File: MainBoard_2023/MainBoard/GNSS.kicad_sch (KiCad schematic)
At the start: 16 parts

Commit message: 裏面にSDスロットを配置、GPS配置
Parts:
- removed JP4: SolderJumper, Jumper:SolderJumper-3_P2.0mm_Open_TrianglePad1.0x1.5mm_NumberLabels, symbol Jumper:SolderJumper_3_Bridged123
- removed R46, R47: 470, Resistor_SMD:R_0603_1608Metric_Pad0.98x0.95mm_HandSolder, symbol Device:R_Small
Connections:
- net +3.3V: now also R48.2, R49.2
- net RX: now also ANT1.14 (RXD)
- net TX: now also ANT1.13 (TXD)
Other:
- note removed: "Cut Jumper to remove I2C pullups from bus"
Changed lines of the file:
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@@
   (junction (at 146.05 78.74) (diameter 0) (color 0 0 0 0)
   )
+  (junction (at 195.58 73.66) (diameter 0) (color 0 0 0 0)
+  )
   (junction (at 190.5 88.9) (diameter 0) (color 0 0 0 0)
   )
@@
     (stroke (width 0) (type default) (color 0 0 0 0))
   )
-  (wire (pts (xy 195.58 67.31) (xy 195.58 69.85))
+  (wire (pts (xy 195.58 72.39) (xy 195.58 73.66))
     (stroke (width 0) (type default) (color 0 0 0 0))
   )
@@
     (stroke (width 0) (type default) (color 0 0 0 0))
   )
-  (wire (pts (xy 172.72 96.52) (xy 177.8 96.52))
+  (wire (pts (xy 172.72 96.52) (xy 180.34 96.52))
+    (stroke (width 0) (type default) (color 0 0 0 0))
+  )
+  (wire (pts (xy 190.5 73.66) (xy 195.58 73.66))
     (stroke (width 0) (type default) (color 0 0 0 0))
   )
@@
     (stroke (width 0) (type default) (color 0 0 0 0))
   )
-  (wire (pts (xy 182.88 93.98) (xy 185.42 93.98))
-    (stroke (width 0) (type default) (color 0 0 0 0))
-  )
-  (wire (pts (xy 182.88 96.52) (xy 185.42 96.52))
+  (wire (pts (xy 195.58 73.66) (xy 200.66 73.66))
     (stroke (width 0) (type default) (color 0 0 0 0))
   )
@@
     (stroke (width 0) (type default) (color 0 0 0 0))
   )
-  (wire (pts (xy 172.72 93.98) (xy 177.8 93.98))
+  (wire (pts (xy 172.72 93.98) (xy 180.34 93.98))
     (stroke (width 0) (type default) (color 0 0 0 0))
   )
@@
     (effects (font (size 1 1)) (justify left bottom))
   )
-  (text "Cut Jumper to remove\nI2C pullups from bus" (at 176.53 71.12 180)
-    (effects (font (size 1 1)) (justify left bottom))
-  )
   (text "RTC Backup" (at 115.57 62.23 180)
     (effects (font (size 2.54 2.54)) (justify right bottom))
@@
     (effects (font (size 1.27 1.27)) (justify right bottom))
   )
-  (hierarchical_label "TX" (shape passive) (at 185.42 93.98 0)
+  (hierarchical_label "TX" (shape passive) (at 180.34 93.98 0)
     (effects (font (size 1.27 1.27)) (justify left))
   )
@@
     (effects (font (size 1.27 1.27)) (justify left))
   )
-  (hierarchical_label "RX" (shape passive) (at 185.42 96.52 0)
-    (effects (font (size 1.27 1.27)) (justify left))
-  )
-  (symbol (lib_id "Device:R_Small") (at 180.34 96.52 90) (unit 1)
-    (in_bom yes) (on_board yes)
-    (property "Reference" "R47" (id 0) (at 176.53 97.79 90))
-    (property "Value" "470" (id 1) (at 180.34 96.52 90))
-    (property "Footprint" "Resistor_SMD:R_0603_1608Metric_Pad0.98x0.95mm_HandSolder" (id 2) (at 180.34 96.52 0)
-      (effects (font (size 1.27 1.27)) hide)
-    )
-    (property "Datasheet" "~" (id 3) (at 180.34 96.52 0)
-      (effects (font (size 1.27 1.27)) hide)
-    )
-    (pin "1")
-    (pin "2")
-  )
-  (symbol (lib_id "power:+3.3V") (at 195.58 67.31 0) (unit 1)
-    (in_bom yes) (on_board yes)
-    (property "Reference" "#PWR0110" (id 0) (at 195.58 71.12 0)
-      (effects (font (size 1.27 1.27)) hide)
-    )
-    (property "Value" "+3.3V" (id 1) (at 195.58 63.5 0))
-    (property "Footprint" "" (id 2) (at 195.58 67.31 0)
-      (effects (font (size 1.27 1.27)) hide)
-    )
-    (property "Datasheet" "" (id 3) (at 195.58 67.31 0)
+  (hierarchical_label "RX" (shape passive) (at 180.34 96.52 0)
+    (effects (font (size 1.27 1.27)) (justify left))
+  )
+  (symbol (lib_id "power:+3.3V") (at 195.58 72.39 0) (unit 1)
+    (in_bom yes) (on_board yes)
+    (property "Reference" "#PWR0110" (id 0) (at 195.58 76.2 0)
+      (effects (font (size 1.27 1.27)) hide)
+    )
+    (property "Value" "+3.3V" (id 1) (at 195.58 68.58 0))
+    (property "Footprint" "" (id 2) (at 195.58 72.39 0)
+      (effects (font (size 1.27 1.27)) hide)
+    )
+    (property "Datasheet" "" (id 3) (at 195.58 72.39 0)
       (effects (font (size 1.27 1.27)) hide)
     )
@@
     (pin "1")
   )
-  (symbol (lib_id "Device:R_Small") (at 180.34 93.98 90) (unit 1)
-    (in_bom yes) (on_board yes)
-    (property "Reference" "R46" (id 0) (at 176.53 92.71 90))
-    (property "Value" "470" (id 1) (at 180.34 93.98 90))
-    (property "Footprint" "Resistor_SMD:R_0603_1608Metric_Pad0.98x0.95mm_HandSolder" (id 2) (at 180.34 93.98 0)
-      (effects (font (size 1.27 1.27)) hide)
-    )
-    (property "Datasheet" "~" (id 3) (at 180.34 93.98 0)
-      (effects (font (size 1.27 1.27)) hide)
-    )
-    (pin "1")
-    (pin "2")
-  )
-  (symbol (lib_id "Jumper:SolderJumper_3_Bridged123") (at 195.58 73.66 180) (unit 1)
-    (in_bom yes) (on_board yes)
-    (property "Reference" "JP4" (id 0) (at 199.39 69.85 0))
-    (property "Value" "SolderJumper" (id 1) (at 204.47 72.39 0))
-    (property "Footprint" "Jumper:SolderJumper-3_P2.0mm_Open_TrianglePad1.0x1.5mm_NumberLabels" (id 2) (at 195.58 73.66 0)
-      (effects (font (size 1.27 1.27)) hide)
-    )
-    (property "Datasheet" "~" (id 3) (at 195.58 73.66 0)
-      (effects (font (size 1.27 1.27)) hide)
-    )
-    (pin "1")
-    (pin "2")
-    (pin "3")
-  )
   (symbol (lib_id "Device:R_Small") (at 200.66 80.01 180) (unit 1)

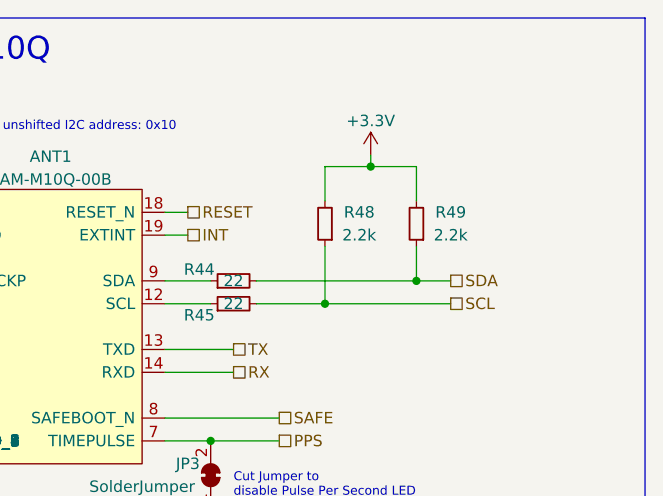
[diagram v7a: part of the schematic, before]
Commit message: 回路図とPCBを変更
RJコネクタに変更
秋月のBNO055に変更
気圧センサのフットプリントを変更
ブロックタイプエミフィルのパッドを縮小
外形と取り付け穴を設定
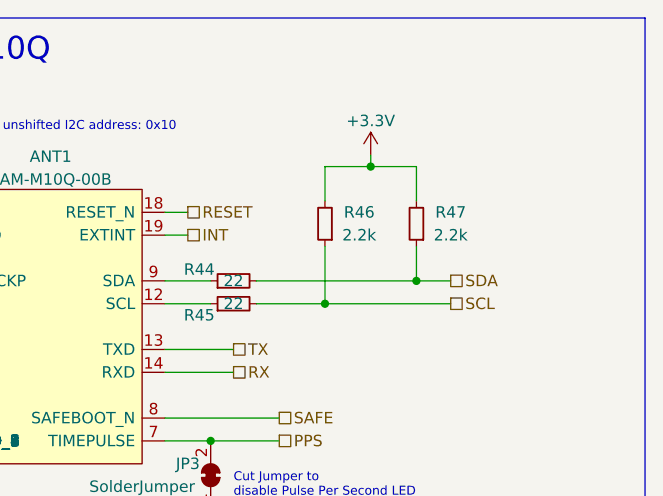
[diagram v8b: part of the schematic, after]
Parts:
- renumbered R48 to R46, R49 to R47
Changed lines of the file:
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@@
   (symbol (lib_id "power:+3.3V") (at 195.58 72.39 0) (unit 1)
     (in_bom yes) (on_board yes)
-    (property "Reference" "#PWR0110" (id 0) (at 195.58 76.2 0)
+    (property "Reference" "#PWR0125" (id 0) (at 195.58 76.2 0)
       (effects (font (size 1.27 1.27)) hide)
     )
@@
   (symbol (lib_id "power:+3.3V") (at 135.89 96.52 0) (unit 1)
     (in_bom yes) (on_board yes)
-    (property "Reference" "#PWR0105" (id 0) (at 135.89 100.33 0)
+    (property "Reference" "#PWR0120" (id 0) (at 135.89 100.33 0)
       (effects (font (size 1.27 1.27)) hide)
     )
@@
   (symbol (lib_id "Device:R_Small") (at 200.66 80.01 180) (unit 1)
     (in_bom yes) (on_board yes)
-    (property "Reference" "R49" (id 0) (at 204.47 78.74 0))
+    (property "Reference" "R47" (id 0) (at 204.47 78.74 0))
     (property "Value" "2.2k" (id 1) (at 204.47 81.28 0))
     (property "Footprint" "Resistor_SMD:R_0603_1608Metric_Pad0.98x0.95mm_HandSolder" (id 2) (at 200.66 80.01 0)
@@
   (symbol (lib_id "power:GND") (at 135.89 106.68 0) (unit 1)
     (in_bom yes) (on_board yes)
-    (property "Reference" "#PWR0106" (id 0) (at 135.89 113.03 0)
+    (property "Reference" "#PWR0121" (id 0) (at 135.89 113.03 0)
       (effects (font (size 1.27 1.27)) hide)
     )
@@
   (symbol (lib_id "power:+3.3V") (at 146.05 76.2 0) (unit 1)
     (in_bom yes) (on_board yes)
-    (property "Reference" "#PWR0107" (id 0) (at 146.05 80.01 0)
+    (property "Reference" "#PWR0122" (id 0) (at 146.05 80.01 0)
       (effects (font (size 1.27 1.27)) hide)
     )
@@
   (symbol (lib_id "power:GND") (at 177.8 121.92 0) (unit 1)
     (in_bom yes) (on_board yes)
-    (property "Reference" "#PWR0109" (id 0) (at 177.8 128.27 0)
+    (property "Reference" "#PWR0124" (id 0) (at 177.8 128.27 0)
       (effects (font (size 1.27 1.27)) hide)
     )
@@
   (symbol (lib_id "power:GND") (at 87.63 90.17 0) (unit 1)
     (in_bom yes) (on_board yes)
-    (property "Reference" "#PWR0103" (id 0) (at 87.63 96.52 0)
+    (property "Reference" "#PWR0118" (id 0) (at 87.63 96.52 0)
       (effects (font (size 1.27 1.27)) hide)
     )
@@
   (symbol (lib_id "power:GND") (at 146.05 106.68 0) (unit 1)
     (in_bom yes) (on_board yes)
-    (property "Reference" "#PWR0108" (id 0) (at 146.05 113.03 0)
+    (property "Reference" "#PWR0123" (id 0) (at 146.05 113.03 0)
       (effects (font (size 1.27 1.27)) hide)
     )
@@
   (symbol (lib_id "Device:R_Small") (at 190.5 80.01 180) (unit 1)
     (in_bom yes) (on_board yes)
-    (property "Reference" "R48" (id 0) (at 194.31 78.74 0))
+    (property "Reference" "R46" (id 0) (at 194.31 78.74 0))
     (property "Value" "2.2k" (id 1) (at 194.31 81.28 0))
     (property "Footprint" "Resistor_SMD:R_0603_1608Metric_Pad0.98x0.95mm_HandSolder" (id 2) (at 190.5 80.01 0)
@@
   (symbol (lib_id "power:GND") (at 102.87 90.17 0) (unit 1)
     (in_bom yes) (on_board yes)
-    (property "Reference" "#PWR0104" (id 0) (at 102.87 96.52 0)
+    (property "Reference" "#PWR0119" (id 0) (at 102.87 96.52 0)
       (effects (font (size 1.27 1.27)) hide)
     )
@@
   (symbol (lib_id "power:+3.3V") (at 87.63 63.5 0) (unit 1)
     (in_bom yes) (on_board yes)
-    (property "Reference" "#PWR0102" (id 0) (at 87.63 67.31 0)
-      (effects (font (size 1.27 1.27)) hide)
-    )
+    (property "Reference" "#PWR0117" (id 0) (at 87.63 67.31 0)
+      (effects (font (size 1.27 1.27)) hide)
+    )
